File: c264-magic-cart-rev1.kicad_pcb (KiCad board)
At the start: 2 copper layers, 58.4 x 89.5 mm, 10 parts, among them CN1 C16_NEWSTYLE_EXP_PORT, U1 27C080, U2 74HCT273, U3 27C160, U5 GAL20V8

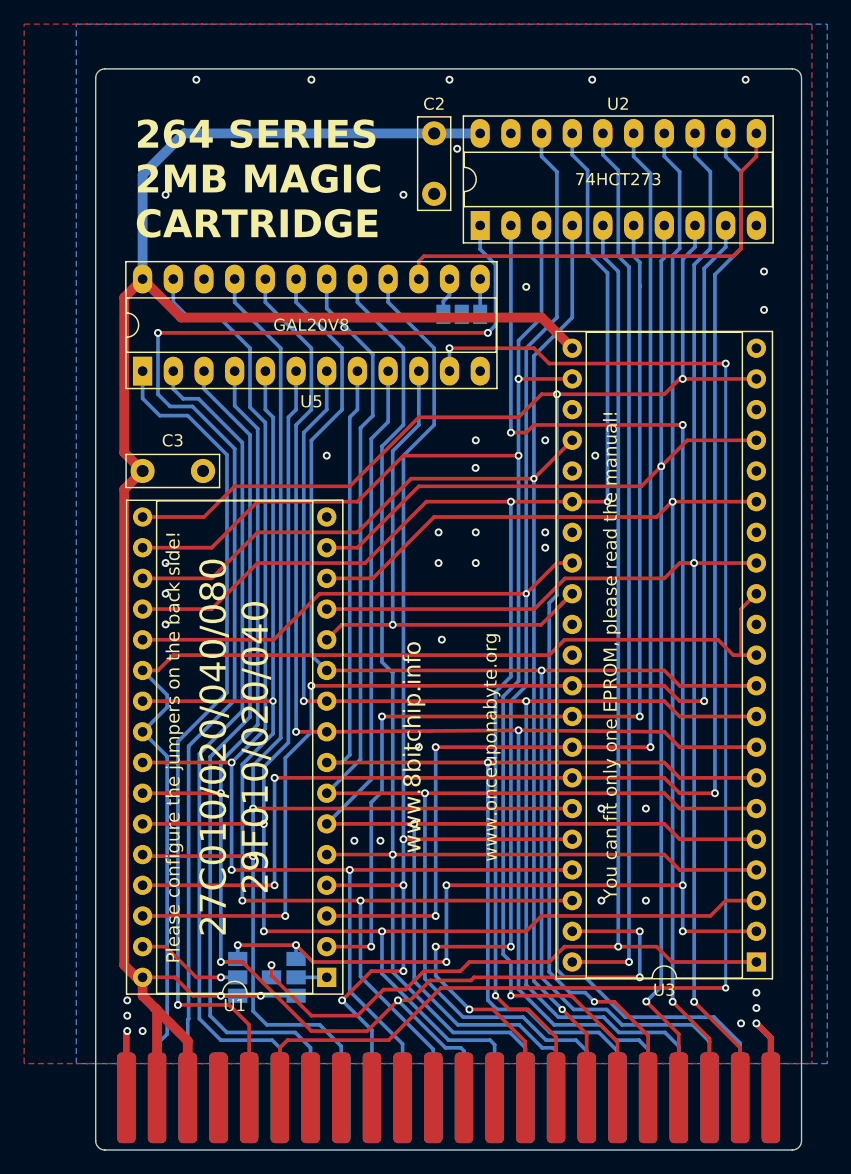
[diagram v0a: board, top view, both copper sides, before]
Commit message: Add cap for U3
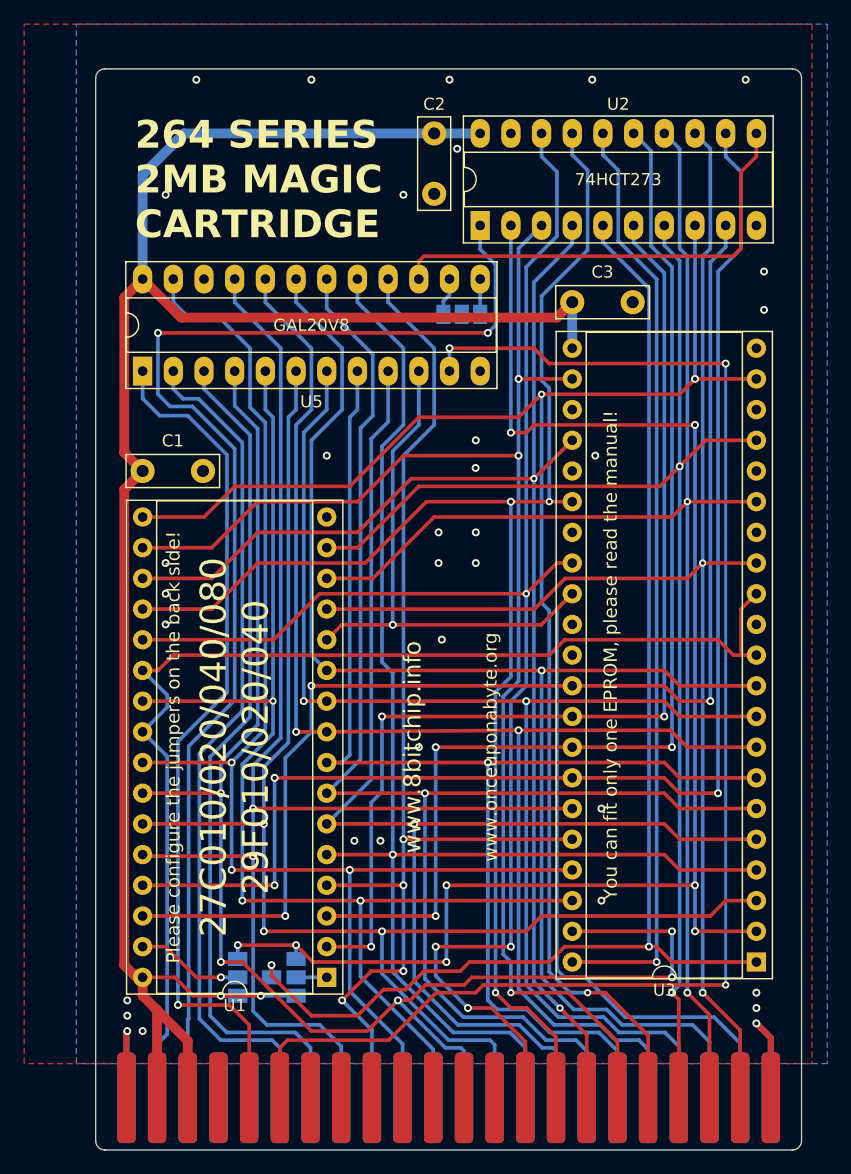
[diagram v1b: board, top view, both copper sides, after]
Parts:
- added C3: 100n, Capacitor_THT:C_Disc_D7.5mm_W2.5mm_P5.00mm, F.Cu at (158.8, 78.7)
- renumbered C3 to C1
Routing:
- net /A9: track 116.8 -> 122.1 mm
- net VCC: track 170.3 -> 173.5 mm
- net /AA20: track 74.2 -> 77.4 mm
- net /AA16: track 85.3 -> 88.2 mm
- net /AA15: track 92.1 -> 94.7 mm
- net /D6: track 126.7 -> 124.8 mm
- net /AA19: track 106.5 -> 107.6 mm
- net /AA18: track 125.7 -> 126.7 mm
- net /D2: track 113.2 -> 112.5 mm
- net /D0: track 119.7 -> 119.0 mm
- net /D1: track 120.1 -> 119.6 mm
- net GND: vias 41 -> 34

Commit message: Update silkscreen
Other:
- board text added: "https://github.com/SukkoPera/c264-magic-cart-44pin"
- board text removed: "https://github.com/msolajic/c264-magic-cart"
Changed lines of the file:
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@@
 	(paper "A4")
 	(title_block
+		(title "c264-magic-cart (44-Pin Version)")
 		(date "2026-07-27")
 		(rev "1s")
+		(company "SukkoPera")
+		(comment 1 "Licensed under CERN OHL v.1.2")
+		(comment 2 "https://github.com/SukkoPera/c264-magic-cart-44pin")
 	)
 	(layers
@@
 		)
 	)
-	(gr_text "Hardware Design: Marko Šolajić\n44-Pin Version: SukkoPera\nGenerator Software: Žarko Živanov"
-		(at 153.3429 111.125 -90)
+	(gr_text "Hardware Design: Marko Šolajić\n\n44-Pin Version: SukkoPera\n\nGenerator Software: Žarko Živanov"
+		(at 148.59 111.125 270)
 		(layer "B.SilkS")
 		(effects
@@
 		)
 	)
-	(gr_text "https://github.com/msolajic/c264-magic-cart"
-		(at 169.545 106.68 -90)
+	(gr_text "https://github.com/SukkoPera/c264-magic-cart-44pin"
+		(at 168.926082 106.68 270)
 		(layer "B.SilkS")
 		(effects
 			(font
-				(size 1.7 1.7)
-				(thickness 0.32766)
+				(size 1.4 1.4)
+				(thickness 0.25)
+				(bold yes)
 			)
 			(justify mirror)
@@
 	)
 	(gr_text "Open Hardware licensed under the CERN OHL v. 1.2."
-		(at 166.37 106.68 270)
+		(at 163.609166 106.68 270)
 		(layer "B.SilkS")
 		(effects

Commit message: Get rid of jumper footprints
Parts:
- removed CONFIG0, SJ1: SJ2W, c264-magic-cart-rev1:SJ_2
- added JP1: CONFIG, Jumper:SolderJumper-3_P1.3mm_Open_Pad1.0x1.5mm, B.Cu at (149.9, 79.6)
- added JP2: ROMSEL_1, Jumper:SolderJumper-3_P1.3mm_Open_Pad1.0x1.5mm, B.Cu at (131.1, 134.6)
- JP3: renamed from U$2; value SJ3 -> ROMSEL_2

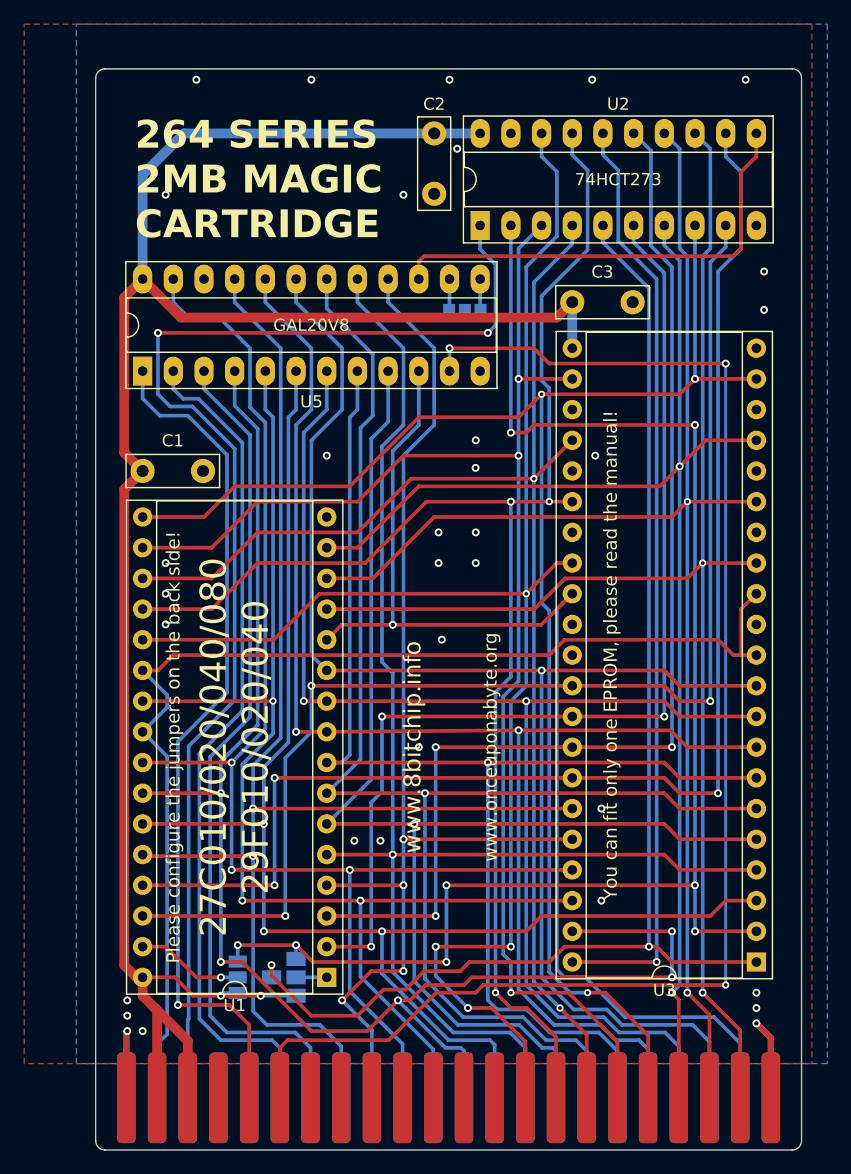
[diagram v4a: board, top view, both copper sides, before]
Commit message: Add bank selection jumpers
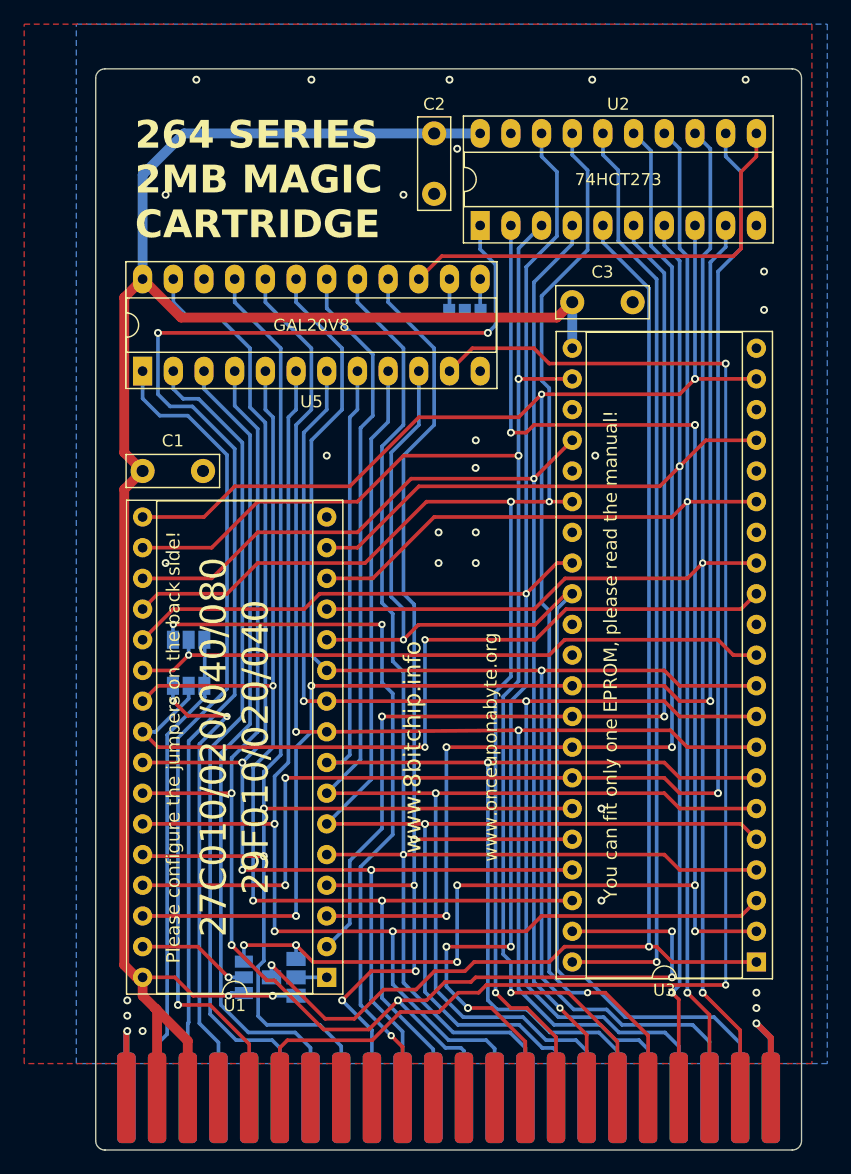
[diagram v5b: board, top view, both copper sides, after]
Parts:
- added JP4: CONFIG, Jumper:SolderJumper-3_P1.3mm_Open_Pad1.0x1.5mm, B.Cu at (127.0, 106.7)
- added JP5: CONFIG, Jumper:SolderJumper-3_P1.3mm_Open_Pad1.0x1.5mm, B.Cu at (127.0, 110.5)
- moved JP2 0.51 mm to (131.6, 134.6)
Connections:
- CN1 pad 10: unconnected-(CN1-~{CS0}-Pad10) -> /~{cs0}
- CN1 pad D: unconnected-(CN1-~{C2}-PadD) -> /~{c2}
- U1 pad 22: /C1LO -> /rom_ce
- U1 pad 24: /C1LO -> /rom_oe
- U3 pad 11: /C1LO -> /rom_ce
- U3 pad 13: /C1LO -> /rom_oe
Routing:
- net /rom_oe: track 0.00 -> 67.8 mm, vias 0 -> 2
- net /~{cs0}: track 0.00 -> 60.7 mm, vias 0 -> 3
- net /C1LO: track 96.2 -> 39.5 mm
- net /rom_ce: track 0.00 -> 53.6 mm, vias 0 -> 1
- net /~{c2}: track 0.00 -> 39.4 mm, vias 0 -> 2
- net /AA16: track 88.2 -> 86.0 mm, vias 3 -> 2
- net /A14: track 69.8 -> 68.1 mm
- net /A15: track 70.0 -> 68.5 mm
- net /A12: track 95.4 -> 96.8 mm
- net /A10: track 102.0 -> 100.6 mm
- net /A9: track 122.1 -> 120.8 mm
- net /D7: track 130.6 -> 129.3 mm
- net /A0: track 97.6 -> 98.8 mm
- net /PHI2: track 119.9 -> 118.8 mm, vias 3 -> 2
- net /A11: track 110.9 -> 109.8 mm
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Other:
- board text added: "ADDRESS DECODER CONFIG (JP1)"
- board text added: "BANK CONFIG (JP4/JP5)"
- board text added: "C1"
- board text added: "C2"
- board text added: "ROM TYPE CONFIG (JP2/JP3)"
- board text added: "~{C1LO}"
- board text added: "~{C2}"
- board text added: "~{CSO}"
- board text removed: "ADDRESS DECODER CONFIGURATION"
- board text removed: "JUMPER CONFIG"
